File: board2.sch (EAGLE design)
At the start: 74 parts, among them Q1 7.68M, Q2 16MHz

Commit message: Created board2 as version 2
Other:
- note added: "Measuring PCB v2.0"
- note removed: "Measuring PCB v1"
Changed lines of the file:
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@@
 <text x="-5.08" y="-175.26" size="5.08" layer="98">Standalone Arduino (atmega328)</text>
 <text x="327.66" y="-175.26" size="5.08" layer="98">Connectors</text>
-<text x="406.4" y="-228.6" size="6.4516" layer="98">Measuring PCB v1</text>
+<text x="406.4" y="-228.6" size="6.4516" layer="98">Measuring PCB v2.0</text>
 <wire x1="370.84" y1="-281.94" x2="370.84" y2="-248.92" width="0.1524" layer="98"/>
 <wire x1="370.84" y1="-248.92" x2="370.84" y2="-233.68" width="0.1524" layer="98"/>

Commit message: Version2: Placed all parts on the board. Still I have to decide about type of connectors etc and route everything
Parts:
- C18, C19, C20, C21, C22, C23, C24, C25, C26, C27, C28, C29, C30, C31, C32, C33, C34: device SparkFun-Capacitors:CAP1206 -> adafruit:C-USC3216
- R10, R11, R2, R3, R4, R5, R9: device SparkFun-Passives:RESISTOR1206 -> adafruit:R-US_R3216
- R6, R7, R8: device adafruit:R-US_M3216 -> adafruit:R-US_R3216
- TO_MASTER_BOARD: device pinhead:PINHD-1X8/90 -> pinhead:PINHD-1X8
- renumbered JP1 to 1WIRE_BUS
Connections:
- net IN1: now also TO_MASTER_BOARD.3; no longer TO_MASTER_BOARD.5
- net IN2: now also TO_MASTER_BOARD.4; no longer TO_MASTER_BOARD.6
- net OUT1: now also TO_MASTER_BOARD.5; no longer TO_MASTER_BOARD.7
- net OUT2: now also TO_MASTER_BOARD.6; no longer TO_MASTER_BOARD.8
- net SCL: now also TO_MASTER_BOARD.8; no longer TO_MASTER_BOARD.4
- net SDA: now also TO_MASTER_BOARD.7; no longer TO_MASTER_BOARD.3
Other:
- moved on the sheet: C18, C19, C20, C21, C22, C23, C24, C25, C26, C27, C28, C29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

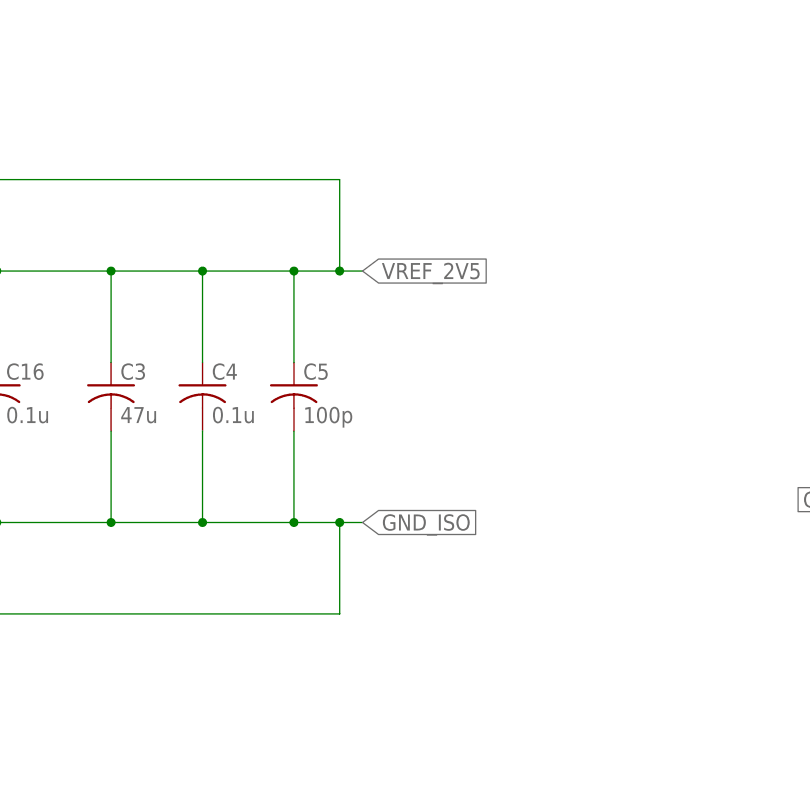
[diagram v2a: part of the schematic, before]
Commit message: Added GND planes and continue working on tracing..
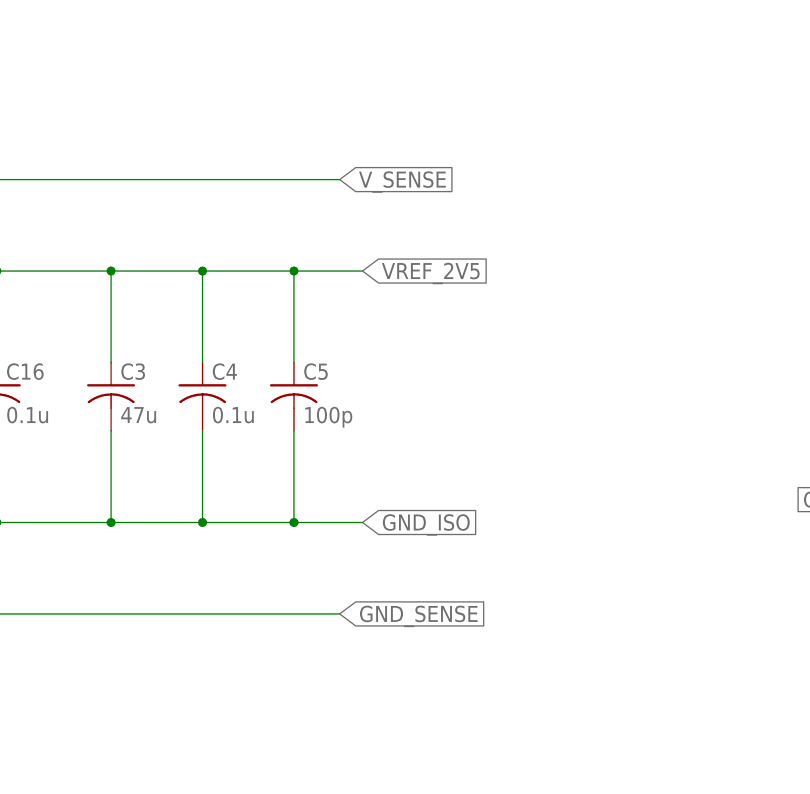
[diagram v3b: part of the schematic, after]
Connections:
- new net GND_SENSE: 2V5_VOLTAGE_REF.GND_SEN
- new net V_SENSE: 2V5_VOLTAGE_REF.VOUT_SEN
- net GND_ISO: no longer 2V5_VOLTAGE_REF.GND_SEN
- net VREF_2V5: no longer 2V5_VOLTAGE_REF.VOUT_SEN
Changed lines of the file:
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@@
 <wire x1="281.94" y1="-134.62" x2="281.94" y2="-144.78" width="0.1524" layer="91"/>
 <junction x="281.94" y="-144.78"/>
-<wire x1="281.94" y1="-144.78" x2="287.02" y2="-144.78" width="0.1524" layer="91"/>
-<wire x1="287.02" y1="-144.78" x2="289.56" y2="-144.78" width="0.1524" layer="91"/>
+<wire x1="281.94" y1="-144.78" x2="289.56" y2="-144.78" width="0.1524" layer="91"/>
 <wire x1="271.78" y1="-144.78" x2="281.94" y2="-144.78" width="0.1524" layer="91"/>
 <pinref part="C4" gate="G$1" pin="2"/>
@@
 <label x="289.56" y="-144.78" size="1.778" layer="95" xref="yes"/>
 <junction x="261.62" y="-144.78"/>
-<pinref part="2V5_VOLTAGE_REF" gate="A" pin="GND_SEN"/>
-<wire x1="198.12" y1="-129.54" x2="193.04" y2="-129.54" width="0.1524" layer="91"/>
-<wire x1="193.04" y1="-129.54" x2="193.04" y2="-154.94" width="0.1524" layer="91"/>
-<wire x1="193.04" y1="-154.94" x2="287.02" y2="-154.94" width="0.1524" layer="91"/>
-<wire x1="287.02" y1="-154.94" x2="287.02" y2="-144.78" width="0.1524" layer="91"/>
-<junction x="287.02" y="-144.78"/>
 <wire x1="248.92" y1="-144.78" x2="261.62" y2="-144.78" width="0.1524" layer="91"/>
 </segment>
@@
 <net name="VREF_2V5" class="0">
 <segment>
-<pinref part="2V5_VOLTAGE_REF" gate="A" pin="VOUT_SEN"/>
-<wire x1="198.12" y1="-127" x2="193.04" y2="-127" width="0.1524" layer="91"/>
-<wire x1="193.04" y1="-127" x2="193.04" y2="-106.68" width="0.1524" layer="91"/>
-<wire x1="193.04" y1="-106.68" x2="287.02" y2="-106.68" width="0.1524" layer="91"/>
+<wire x1="241.3" y1="-20.32" x2="226.06" y2="-20.32" width="0.1524" layer="91"/>
+<label x="226.06" y="-20.32" size="1.778" layer="95" rot="R180" xref="yes"/>
+<pinref part="ADC" gate="A" pin="VREFP"/>
+</segment>
+<segment>
 <pinref part="C5" gate="G$1" pin="1"/>
 <wire x1="281.94" y1="-127" x2="281.94" y2="-116.84" width="0.1524" layer="91"/>
 <junction x="281.94" y="-116.84"/>
-<wire x1="281.94" y1="-116.84" x2="287.02" y2="-116.84" width="0.1524" layer="91"/>
-<wire x1="287.02" y1="-116.84" x2="289.56" y2="-116.84" width="0.1524" layer="91"/>
+<wire x1="281.94" y1="-116.84" x2="289.56" y2="-116.84" width="0.1524" layer="91"/>
 <wire x1="271.78" y1="-116.84" x2="281.94" y2="-116.84" width="0.1524" layer="91"/>
 <pinref part="C4" gate="G$1" pin="1"/>
@@
 <pinref part="C3" gate="G$1" pin="1"/>
 <wire x1="261.62" y1="-127" x2="261.62" y2="-116.84" width="0.1524" layer="91"/>
-<label x="289.56" y="-116.84" size="1.778" layer="95" xref="yes"/>
-<wire x1="287.02" y1="-106.68" x2="287.02" y2="-116.84" width="0.1524" layer="91"/>
-<junction x="287.02" y="-116.84"/>
 <junction x="261.62" y="-116.84"/>
 <pinref part="2V5_VOLTAGE_REF" gate="A" pin="VOUT_FORCE"/>
 <wire x1="243.84" y1="-116.84" x2="248.92" y2="-116.84" width="0.1524" layer="91"/>
+<junction x="248.92" y="-116.84"/>
+<wire x1="248.92" y1="-116.84" x2="261.62" y2="-116.84" width="0.1524" layer="91"/>
 <pinref part="C16" gate="G$1" pin="1"/>
 <wire x1="248.92" y1="-127" x2="248.92" y2="-116.84" width="0.1524" layer="91"/>
-<junction x="248.92" y="-116.84"/>
-<wire x1="248.92" y1="-116.84" x2="261.62" y2="-116.84" width="0.1524" layer="91"/>
-</segment>
-<segment>
-<wire x1="241.3" y1="-20.32" x2="226.06" y2="-20.32" width="0.1524" layer="91"/>
-<label x="226.06" y="-20.32" size="1.778" layer="95" rot="R180" xref="yes"/>
-<pinref part="ADC" gate="A" pin="VREFP"/>
+<label x="289.56" y="-116.84" size="1.778" layer="95" xref="yes"/>
 </segment>
 </net>
@@
 </segment>
 </net>
+<net name="GND_SENSE" class="0">
+<segment>
+<pinref part="2V5_VOLTAGE_REF" gate="A" pin="GND_SEN"/>
+<wire x1="198.12" y1="-129.54" x2="193.04" y2="-129.54" width="0.1524" layer="91"/>
+<wire x1="193.04" y1="-129.54" x2="193.04" y2="-154.94" width="0.1524" layer="91"/>
+<wire x1="193.04" y1="-154.94" x2="287.02" y2="-154.94" width="0.1524" layer="91"/>
+<label x="287.02" y="-154.94" size="1.778" layer="95" xref="yes"/>
+</segment>
+</net>
+<net name="V_SENSE" class="0">
+<segment>
+<pinref part="2V5_VOLTAGE_REF" gate="A" pin="VOUT_SEN"/>
+<wire x1="198.12" y1="-127" x2="193.04" y2="-127" width="0.1524" layer="91"/>
+<wire x1="193.04" y1="-127" x2="193.04" y2="-106.68" width="0.1524" layer="91"/>
+<wire x1="193.04" y1="-106.68" x2="287.02" y2="-106.68" width="0.1524" layer="91"/>
+<label x="287.02" y="-106.68" size="1.778" layer="95" xref="yes"/>
+</segment>
+</net>

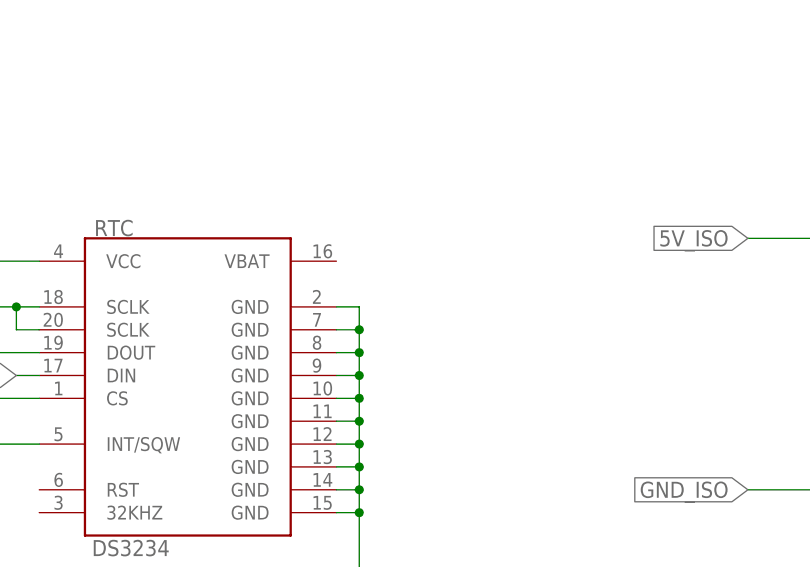
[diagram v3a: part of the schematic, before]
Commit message: added battery for RTC and small changes
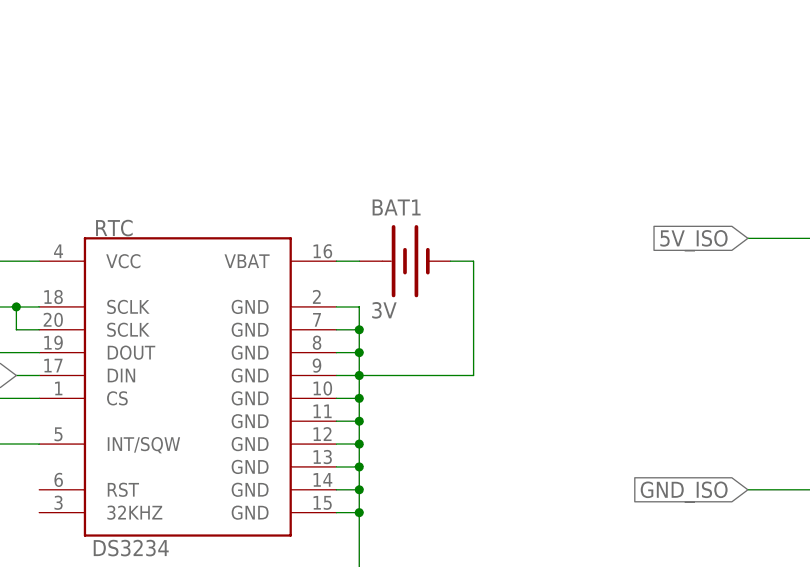
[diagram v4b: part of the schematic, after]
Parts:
- added BAT1: 3V, SparkFun-Electromechanical:BATTERY12MM
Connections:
- new net N$22: BAT1.+, RTC.VBAT
- net GND_ISO: now also BAT1.-
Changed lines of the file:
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@@
 <part name="R11" library="adafruit" deviceset="R-US_" device="R3216" value="10k"/>
 <part name="1WIRE_BUS" library="adafruit" deviceset="PINHD-1X3" device=""/>
+<part name="BAT1" library="SparkFun-Electromechanical" deviceset="BATTERY" device="12MM" value="3V"/>
 </parts>
 <sheets>
@@
 <instance part="R11" gate="G$1" x="147.32" y="-208.28"/>
 <instance part="1WIRE_BUS" gate="A" x="375.92" y="-193.04"/>
+<instance part="BAT1" gate="G$1" x="127" y="-119.38"/>
 </instances>
 <busses>
@@
 <junction x="33.02" y="-132.08"/>
 <label x="25.4" y="-132.08" size="1.778" layer="95" rot="R180" xref="yes"/>
+<pinref part="BAT1" gate="G$1" pin="-"/>
+<wire x1="132.08" y1="-119.38" x2="134.62" y2="-119.38" width="0.1524" layer="91"/>
+<wire x1="134.62" y1="-119.38" x2="134.62" y2="-132.08" width="0.1524" layer="91"/>
+<wire x1="134.62" y1="-132.08" x2="121.92" y2="-132.08" width="0.1524" layer="91"/>
 </segment>
 <segment>
@@
 </segment>
 </net>
+<net name="N$22" class="0">
+<segment>
+<pinref part="BAT1" gate="G$1" pin="+"/>
+<pinref part="RTC" gate="G$1" pin="VBAT"/>
+<wire x1="121.92" y1="-119.38" x2="119.38" y2="-119.38" width="0.1524" layer="91"/>
+</segment>
+</net>

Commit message: Fixed the fuse footprint
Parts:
- F1: device fuse:SHK20L -> fuse:SHK20L_PAS
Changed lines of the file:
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@@
 <part name="R3B" library="adafruit" deviceset="R-US_" device="M3216" value="1k"/>
 <part name="R1" library="LVK25" deviceset="LVK25" device="R001" value="0.005"/>
-<part name="F1" library="fuse" deviceset="SHK20L" device="" value="15A"/>
+<part name="F1" library="fuse" deviceset="SHK20L_PAS" device="" value="15A"/>
 <part name="C14" library="adafruit" deviceset="C-US" device="C3216" value="0.1u"/>
 <part name="C15" library="adafruit" deviceset="C-US" device="C3216" value="100p"/>
@@
 </segment>
 </net>
-<net name="N$22" class="0">
+<net name="N$15" class="0">
 <segment>
 <pinref part="BAT1" gate="G$1" pin="+"/>

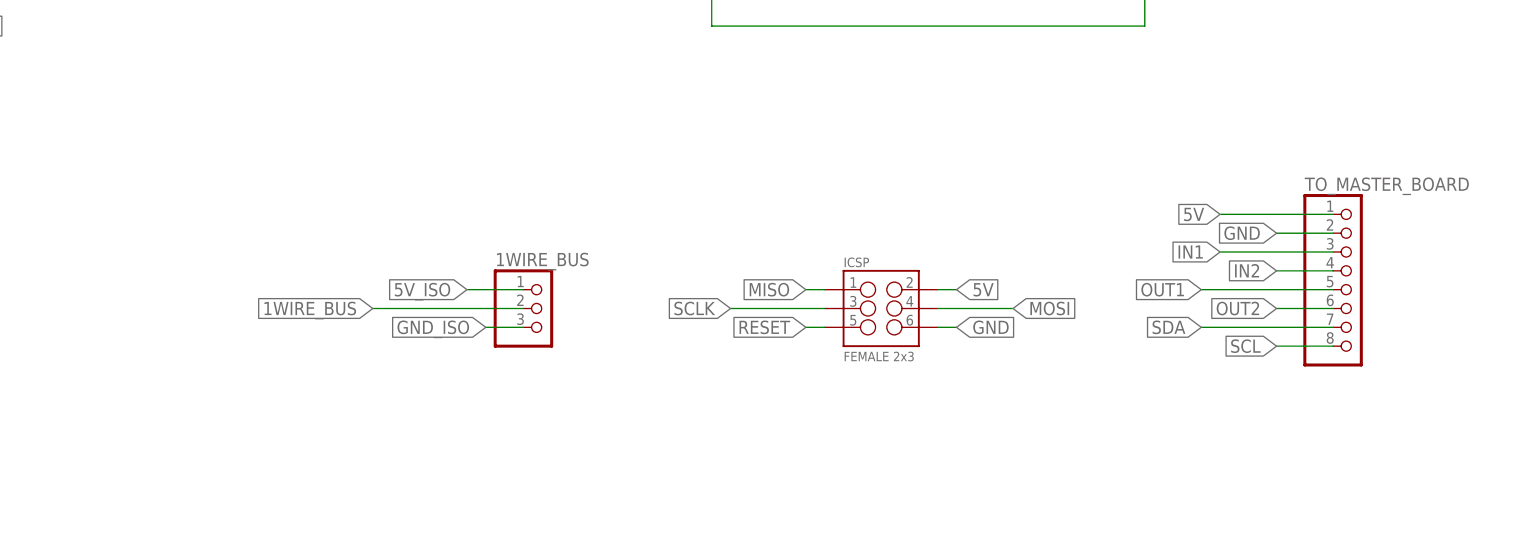
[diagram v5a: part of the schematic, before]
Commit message: Added: connector bypassing isolation, mounting holes
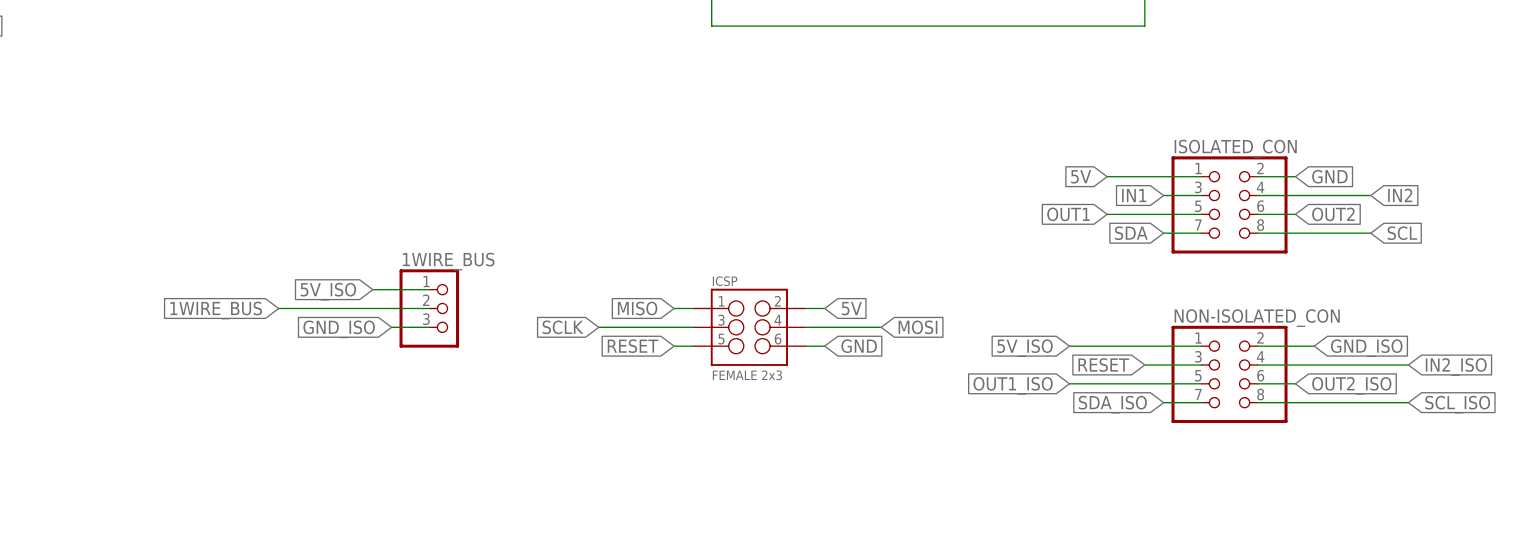
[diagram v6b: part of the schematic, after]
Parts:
- removed TO_MASTER_BOARD: (no value), pinhead:PINHD-1X8
- added ISOLATED_CON, NON-ISOLATED_CON: (no value), adafruit:PINHD-2X4
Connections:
- net 5V: now also ISOLATED_CON.1; no longer TO_MASTER_BOARD.1
- net 5V_ISO: now also NON-ISOLATED_CON.1
- net GND: now also ISOLATED_CON.2; no longer TO_MASTER_BOARD.2
- net GND_ISO: now also NON-ISOLATED_CON.2
- net IN1: now also ISOLATED_CON.3; no longer TO_MASTER_BOARD.3
- net IN2: now also ISOLATED_CON.4; no longer TO_MASTER_BOARD.4
- net IN2_ISO: now also NON-ISOLATED_CON.4
- net OUT1: now also ISOLATED_CON.5; no longer TO_MASTER_BOARD.5
- net OUT1_ISO: now also NON-ISOLATED_CON.5
- net OUT2: now also ISOLATED_CON.6; no longer TO_MASTER_BOARD.6
- net OUT2_ISO: now also NON-ISOLATED_CON.6
- net RESET: now also NON-ISOLATED_CON.3
- net SCL: now also ISOLATED_CON.8; no longer TO_MASTER_BOARD.8
- net SCL_ISO: now also NON-ISOLATED_CON.8
- net SDA: now also ISOLATED_CON.7; no longer TO_MASTER_BOARD.7
- net SDA_ISO: now also NON-ISOLATED_CON.7
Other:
- moved on the sheet: 1WIRE_BUS, ICSP

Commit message: Finished v2.2
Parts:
- removed 1WIRE_BUS: (no value), adafruit:PINHD-1X3
- added 1WIRE-BUS: PHOENIX-TERMINAL-3PIN, Paschalis_connectors:PHOENIX-TERMINAL-3PIN
- renumbered 2V5_VOLTAGE_REF to ADR3425, 3V3_REGULATOR to LP2985, ADC to ADS1256, DC-DC to ADUM5000, RESET_BUTTON to RESET, RTC to DS3234, SIGNAL_ISOLATOR to MAX14850, SJ1 to SJ1-RST, SJ2 to SJ2-SYNC
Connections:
- net 1WIRE_BUS: now also 1WIRE-BUS.2; no longer 1WIRE_BUS.2
- net 5V_ISO: now also 1WIRE-BUS.1; no longer 1WIRE_BUS.1
- net GND_ISO: now also 1WIRE-BUS.3; no longer 1WIRE_BUS.3
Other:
- note added: "Measuring PCB v2.2"
- note removed: "Measuring PCB v2.0"
- moved on the sheet: ICSP

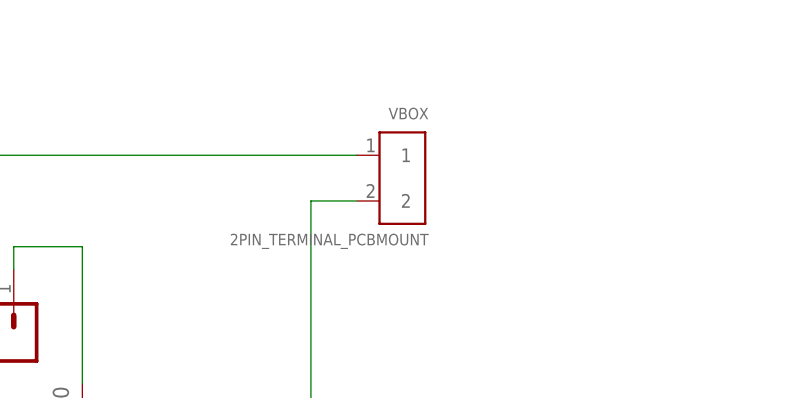
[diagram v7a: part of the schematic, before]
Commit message: Visual changes and clean up
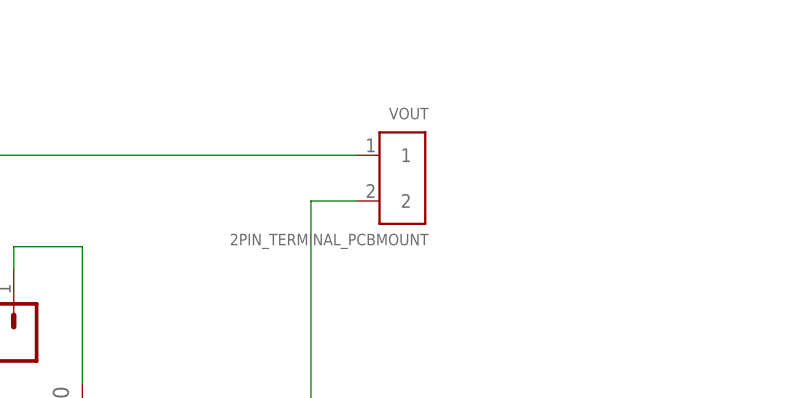
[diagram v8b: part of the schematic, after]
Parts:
- renumbered VBOX to VOUT
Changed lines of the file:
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@@
 <parts>
 <part name="VPANEL" library="TE CONNECTIVITY" deviceset="2PIN_TERMINAL_PCBMOUNT" device=""/>
-<part name="VBOX" library="TE CONNECTIVITY" deviceset="2PIN_TERMINAL_PCBMOUNT" device=""/>
+<part name="VOUT" library="TE CONNECTIVITY" deviceset="2PIN_TERMINAL_PCBMOUNT" device=""/>
 <part name="JP1A" library="SparkFun-Connectors" deviceset="M03" device="PTH"/>
 <part name="JP1B" library="SparkFun-Connectors" deviceset="M03" device="PTH"/>
@@
 <instances>
 <instance part="VPANEL" gate="G$1" x="12.7" y="48.26"/>
-<instance part="VBOX" gate="G$1" x="119.38" y="48.26" rot="MR0"/>
+<instance part="VOUT" gate="G$1" x="119.38" y="48.26" rot="MR0"/>
 <instance part="JP1A" gate="G$1" x="38.1" y="27.94" rot="R90"/>
 <instance part="JP1B" gate="G$1" x="78.74" y="27.94" rot="R90"/>
@@
 <segment>
 <pinref part="VPANEL" gate="G$1" pin="1"/>
-<pinref part="VBOX" gate="G$1" pin="1"/>
+<pinref part="VOUT" gate="G$1" pin="1"/>
 <wire x1="12.7" y1="48.26" x2="38.1" y2="48.26" width="0.1524" layer="91"/>
 <pinref part="JP1A" gate="G$1" pin="2"/>
@@
 <net name="AIN3" class="0">
 <segment>
-<pinref part="VBOX" gate="G$1" pin="2"/>
+<pinref part="VOUT" gate="G$1" pin="2"/>
 <wire x1="119.38" y1="43.18" x2="114.3" y2="43.18" width="0.1524" layer="91"/>
 <wire x1="114.3" y1="43.18" x2="114.3" y2="-35.56" width="0.1524" layer="91"/>
